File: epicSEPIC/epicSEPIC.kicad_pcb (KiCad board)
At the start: 2 copper layers, 46.6 x 80.3 mm, 44 parts, among them J1 Entrada 24V, J2 USB Tipo B, J3 Salida 12-48V, J4 ICSP, Q1 ISZ230N10NM6, U1 PIC18F4550-IML, U2 1EDN7550U, U3 TPS54308, U4 TPS54308, Y1 20M

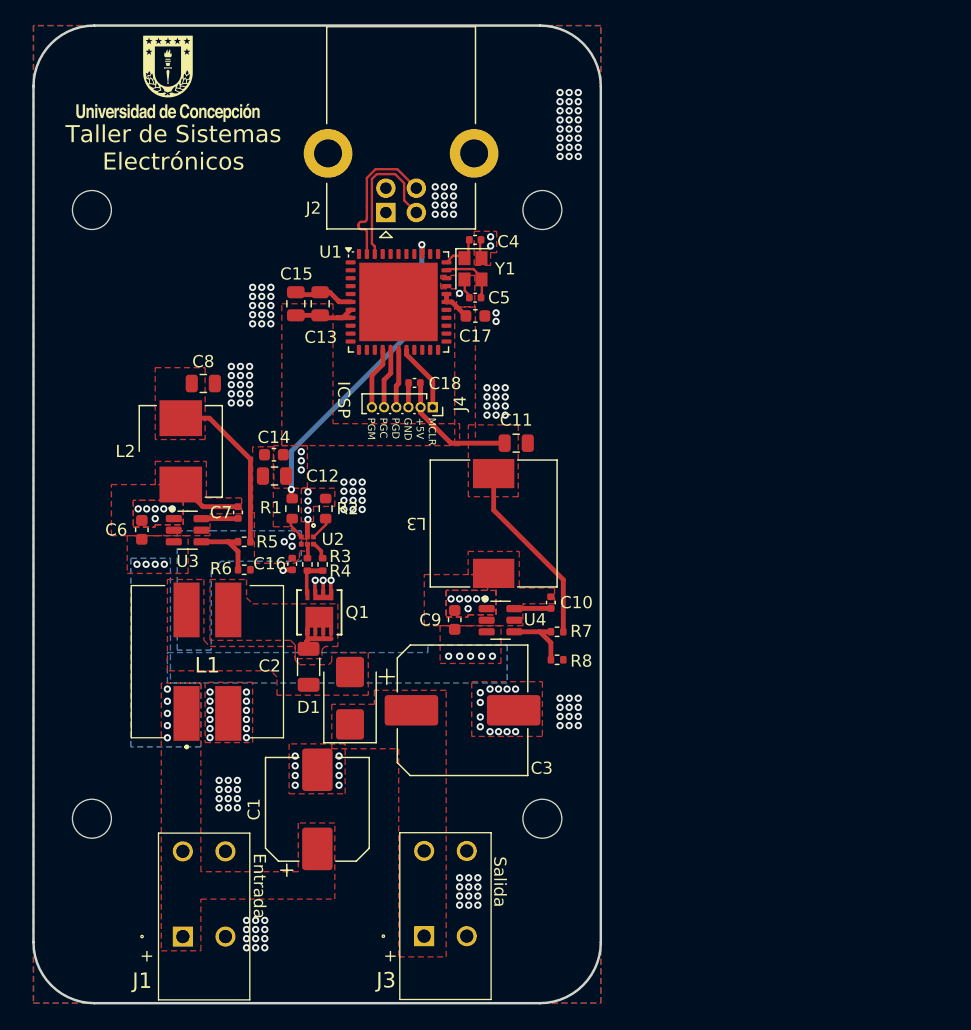
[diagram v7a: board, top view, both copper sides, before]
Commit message: Agregar ESP32 a pcb
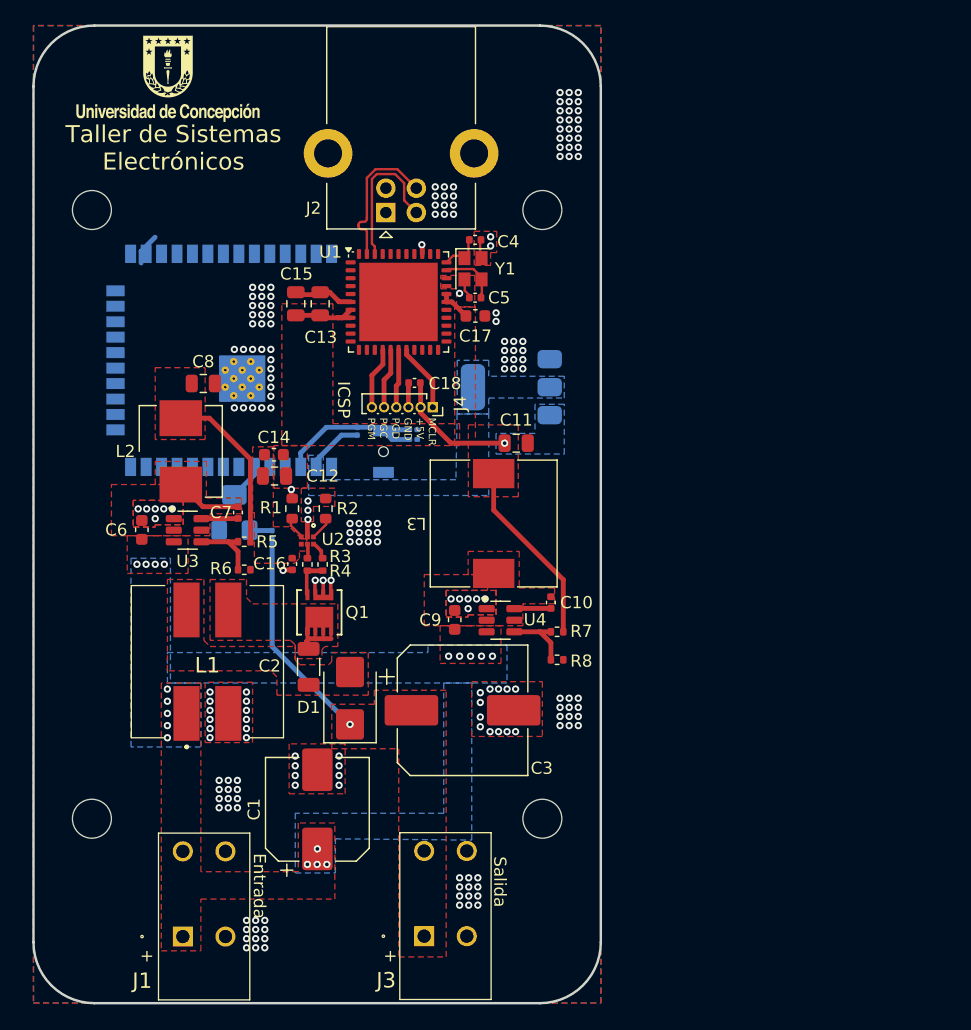
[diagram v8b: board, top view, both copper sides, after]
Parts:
- added C19: 0.1u, Capacitor_SMD:C_0201_0603Metric, B.Cu at (146.2, 99.0)
- added C20: 0.1u, Capacitor_SMD:C_0201_0603Metric, B.Cu at (146.2, 98.2)
- added R10: 10k, Resistor_SMD:R_0201_0603Metric, B.Cu at (141.6, 98.3)
- added R9: 100k, Resistor_SMD:R_0201_0603Metric, B.Cu at (134.6, 106.8)
- added RV1: Radj, Potentiometer_SMD:Potentiometer_Bourns_3224W_Vertical, B.Cu at (131.5, 105.0)
- added SW1: EN, Button_Switch_SMD:SW_SPST_B3U-1000P-B, B.Cu at (143.8, 100.0)
- added U5: ESP32-WROOM-32UE, RF_Module:ESP32-WROOM-32UE, B.Cu at (131.1, 92.5)
- added U7: AMS1117-3.3, Package_TO_SOT_SMD:SOT-223-3_TabPin2, B.Cu at (154.2, 94.7)
- D1: value SK52 -> SK58
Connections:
- net /Potencia/Vout renamed /Monitoreo/Salida
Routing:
- net /Control/PWM: track 26.1 -> 1.56 mm
- net /Monitoreo/Salida: track 0.00 -> 17.9 mm, vias 0 -> 1
- net Net-(U5-EN): track 0.00 -> 13.5 mm
- net +3.3V: track 0.00 -> 4.77 mm
- net Net-(U5-IO34): track 0.00 -> 2.98 mm
- net unconnected-(U5-IO4-Pad26): track 0.00 -> 2.59 mm
- net Net-(R9-Pad2): track 0.00 -> 1.86 mm
- net GND: vias 198 -> 194
- net /Potencia/Vin: vias 14 -> 18
- net +5V: vias 0 -> 1
- net +15V: vias 3 -> 0
- added copper zone on B.Cu, net +3.3V
- added copper zone on B.Cu, net +5V
- removed copper zone on B.Cu, net +15V
